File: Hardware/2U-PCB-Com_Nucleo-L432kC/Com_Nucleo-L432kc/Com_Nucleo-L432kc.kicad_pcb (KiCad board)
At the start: 2 copper layers, 90 x 92 mm, 44 parts, among them IC1 PCI_EXPRESS_CARD, J1 Bus Standard, J2 I2C_Grove, J3 I2C_Grove, J4 Conn_01x08, J5 Conn_01x08, J6 Conn_01x15, J7 Conn_01x15, J8 I2C_Grove, J9 I2C_Grove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

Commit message: correction carte Lucas
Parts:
- removed the G*** at (147.1, 59.4)
- removed JP1: Jumper_RESET_L432KC_Open, Button_Switch_SMD:SW_Push_1P1T_NO_CK_KMR2
- removed JP2: Jumper_MCU_Reset_Open, Button_Switch_SMD:SW_Push_1P1T_NO_CK_KMR2
- removed JP3: Jumper_SX1303_Reset_Open, Button_Switch_SMD:SW_Push_1P1T_NO_CK_KMR2
- removed REF** (x2): MountingHole_3.5mm, MountingHole:MountingHole_3.5mm
- added SW101: Jumper_RESET_L432KC_Open, Button_Switch_THT:SW_PUSH_6mm, F.Cu at (131.7, 56.0)
- added SW102: Jumper_MCU_Reset_Open, Button_Switch_THT:SW_PUSH_6mm, F.Cu at (139.3, 56.0)
- added SW103: Jumper_SX1303_Reset_Open, Button_Switch_THT:SW_PUSH_6mm, F.Cu at (151.4, 49.3)
- B1, B2: moved to F.Cu
- C1, C2, C3, C4, C5, C6: footprint Capacitor_SMD:C_0805_2012Metric -> Capacitor_SMD:C_0805_2012Metric_Pad1.18x1.45mm_HandSolder
- C10, C11, C13, C14, C7, C8, C9: footprint Capacitor_SMD:C_0805_2012Metric -> Capacitor_SMD:C_0805_2012Metric_Pad1.18x1.45mm_HandSolder; moved to F.Cu
- CR1: footprint footprints:SO-8_STM -> Library:SO-8_STM; moved to F.Cu
- J1: footprint flatsat_conn:flatsat_conn -> Library:flatsat_conn
- J4, J5: footprint Conn_mikro:MIkrobus_Connector -> Library:MIkrobus_Connector
- R1, R2, R3, R4, R5, R6, R7: footprint Resistor_SMD:R_0805_2012Metric -> Resistor_SMD:R_0805_2012Metric_Pad1.20x1.40mm_HandSolder
- U1: footprint ul_SN74HC04N:N14 -> Library:N14
- moved J8 64.0 mm to (70.7, 57.6), turned to 0 degrees
- moved J3 59.4 mm to (93.5, 57.6), turned to 0 degrees
- moved J9 55.8 mm to (81.7, 57.6), turned to 0 degrees
- moved J2 46.4 mm to (79.0, 51.0)
- moved C7 13.7 mm to (135.9, 60.6), turned to -90 degrees
- moved C8 13.7 mm to (132.9, 60.6), turned to -90 degrees
- moved JP4 9.25 mm to (134.2, 107.6), turned to -90 degrees
- moved C13 7.33 mm to (74.4, 87.2), turned to 0 degrees
- moved C10 7.30 mm to (117.7, 94.6), turned to -90 degrees
- moved C14 7.29 mm to (74.5, 89.8), turned to 0 degrees
- moved C9 5.85 mm to (115.4, 94.6), turned to -90 degrees
- moved C11 5.56 mm to (133.9, 114.1), turned to -90 degrees
- moved CR1 5.38 mm to (116.2, 88.5)
- moved JP5 2.72 mm to (131.2, 99.4), turned to 90 degrees
- moved C6 2.04 mm to (127.4, 105.9), turned to 90 degrees
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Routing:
- net /MCU_NRESET: track 290.8 -> 230.0 mm, vias 1 -> 3
- net GND: track 69.3 -> 17.8 mm, vias 13 -> 91
- net +3V3: track 335.6 -> 367.0 mm, vias 1 -> 0
- net /SCL: track 195.1 -> 165.4 mm, vias 1 -> 3
- net /CS_MCU: track 156.6 -> 137.6 mm
- net /MCU_MOSI: track 98.5 -> 116.4 mm, vias 0 -> 3
- net Net-(B2-OE): track 115.0 -> 97.5 mm, vias 0 -> 1
- net /CAN1_TX: track 45.7 -> 28.3 mm, vias 0 -> 1
- net /Vin: track 88.6 -> 74.6 mm
- net /HOST_SCK: track 147.2 -> 135.0 mm
- net Net-(CR1-ASC): track 11.6 -> 23.5 mm
- net /SDA: track 169.8 -> 158.6 mm, vias 1 -> 2
- net /CAN_TD: track 32.9 -> 21.9 mm
- net /TH1: track 91.8 -> 81.7 mm
- net /RX_CALC: track 69.8 -> 60.7 mm
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
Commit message: reprise de la serigraphie
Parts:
- added G***: LOGO, Com Nucleo library:logo_csug, F.Cu at (82.0, 108.9)

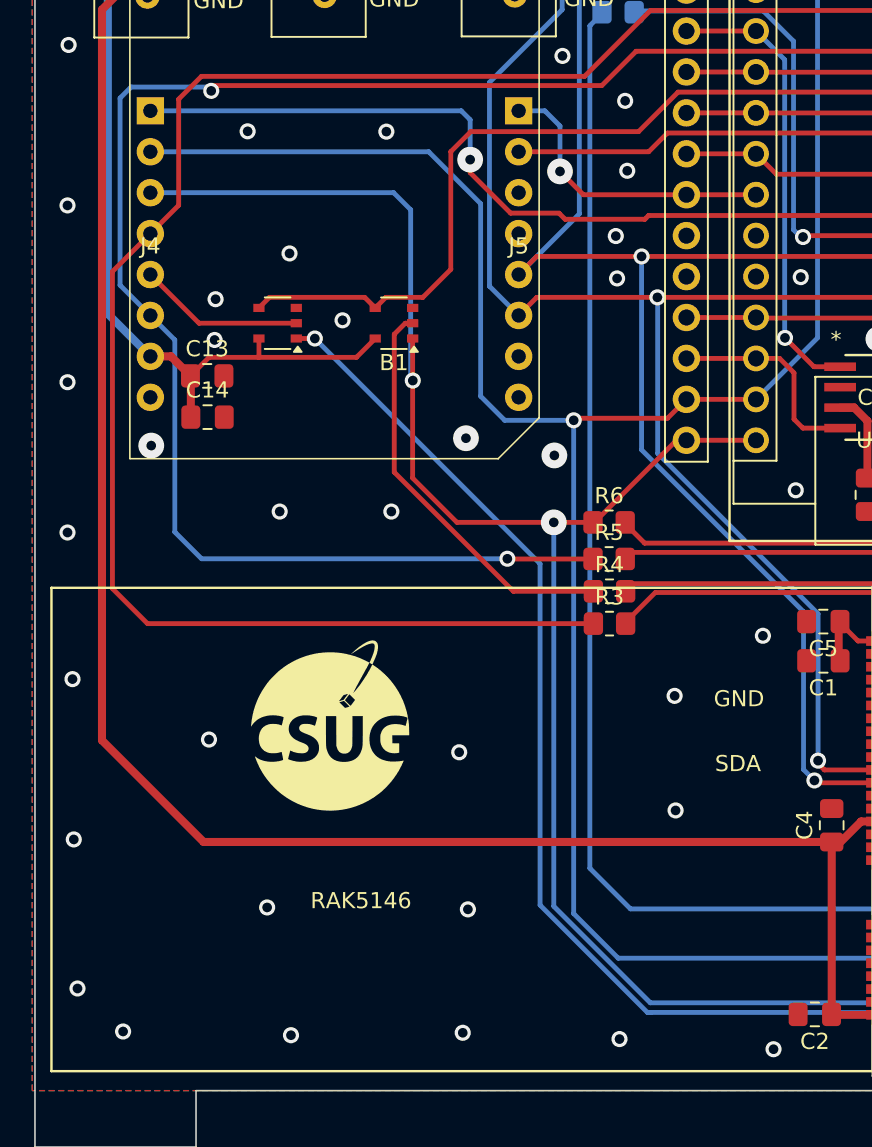
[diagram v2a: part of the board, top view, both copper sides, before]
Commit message: peaufinage serigraphie et tracage fichiers de fabrication pour commande JLCPCB
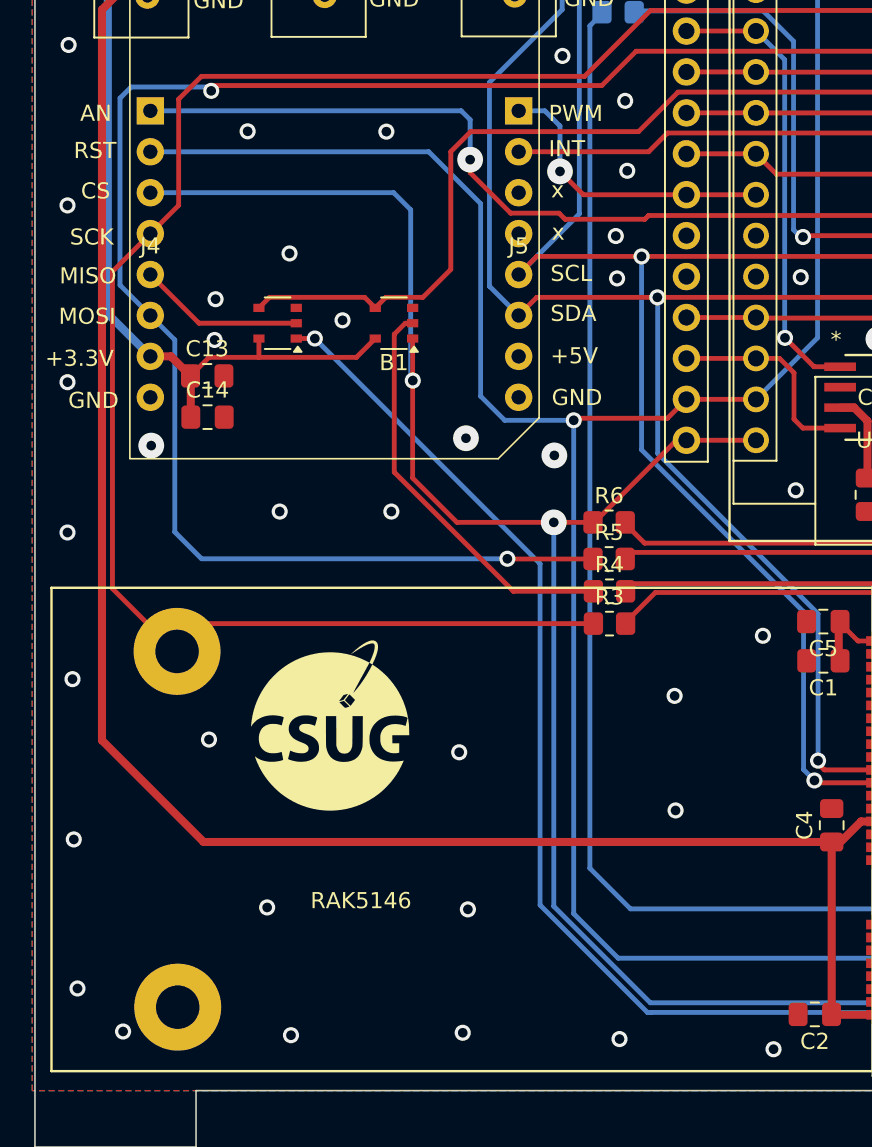
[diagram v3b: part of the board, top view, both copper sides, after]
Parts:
- added G***: LOGO, Com Nucleo library:logo_csug, B.Cu at (123.1, 109.8)
- added QR: LOGO, Com Nucleo library:qr_code_flatsat, B.Cu at (82.2, 80.7)
- added REF**: MountingHole_2.7mm_M2.5_Pad, MountingHole:MountingHole_2.7mm_M2.5_Pad, F.Cu at (72.6, 126.4)
- added REF**: MountingHole_2.7mm_M2.5_Pad, MountingHole:MountingHole_2.7mm_M2.5_Pad, F.Cu at (72.6, 104.3)
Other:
- board text added: "+3.3V"
- board text added: "+5V"
- board text added: "AMI-CMA COMETES"
- board text added: "AMI-CMA FAME"
- board text added: "AN"
- board text added: "CS"
- board text added: "INT"
- board text added: "MISO"
- board text added: "MOSI"
- board text added: "PWM"
- board text added: "Persyval Lab - LSI Carnot"
- board text added: "RST"
- board text added: "S/N :"
- board text added: "SCK"
- board text added: "Tested :"
- board text added: "Thingsat Board for INISAT"
- board text added: "x"
